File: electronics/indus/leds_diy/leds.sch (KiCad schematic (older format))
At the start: 21 parts, among them P1 LED+, P2 THERM, P3 LED-

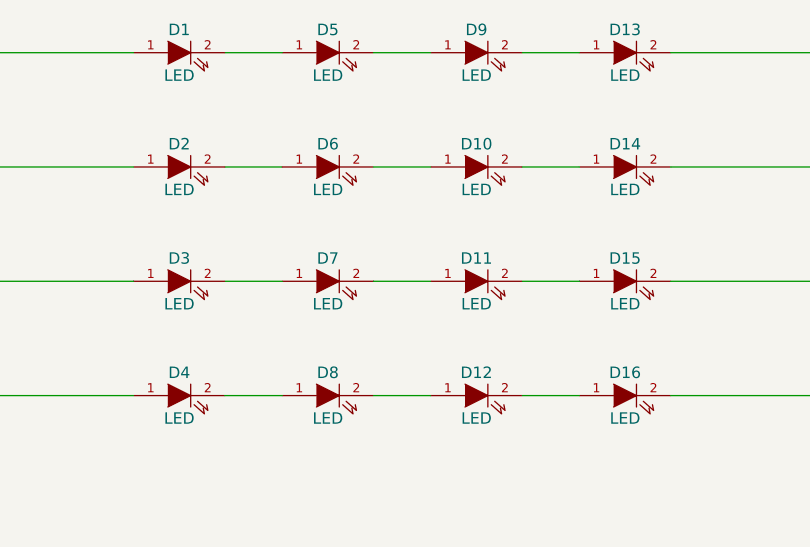
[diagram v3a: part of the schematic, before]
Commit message: led routing - one done
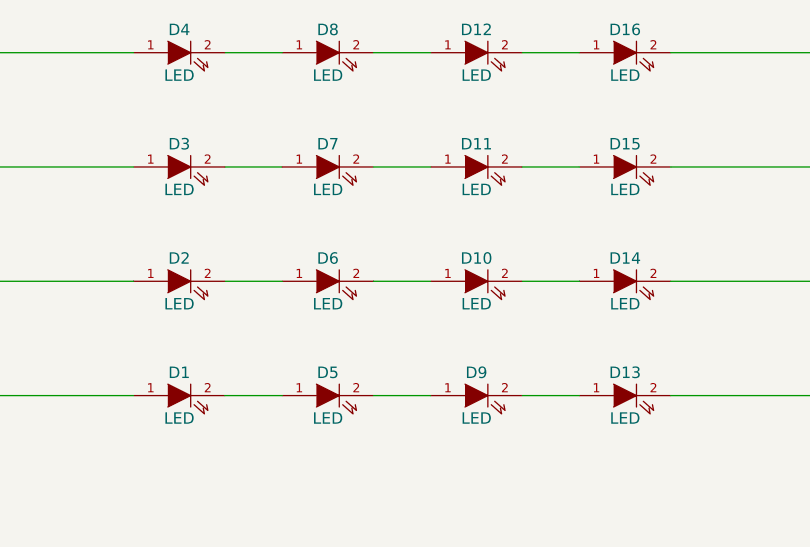
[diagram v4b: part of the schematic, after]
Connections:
- net at D1.1 (A): now also P1.1 (P1); no longer P1.4 (P4)
- net at D13.2 (K): now also P3.4 (P4); no longer P3.1 (P1)
- net at D2.1 (A): now also P1.2 (P2); no longer P1.3 (P3)
- net at D14.2 (K): now also P3.3 (P3); no longer P3.2 (P2)
- net at D3.1 (A): now also P1.3 (P3); no longer P1.2 (P2)
- net at D15.2 (K): now also P3.2 (P2); no longer P3.3 (P3)
- net at D4.1 (A): now also P1.4 (P4); no longer P1.1 (P1)
- net at D16.2 (K): now also P3.1 (P1); no longer P3.4 (P4)
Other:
- moved on the sheet: D1, D10, D11, D12, D13, D14, D15, D16, D2, D3, D4, D5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
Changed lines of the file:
@@
 L LED-RESCUE-leds D1
 U 1 1 56E1A1EF
+P 4750 3450
+F 0 "D1" H 4750 3550 50  0000 C CNN
+F 1 "LED" H 4750 3350 50  0000 C CNN
+F 2 "risebox:LUXEON-C" H 4750 3450 60  0001 C CNN
+F 3 "" H 4750 3450 60  0000 C CNN
+	1    4750 3450
+	1    0    0    -1
+$EndComp
+$Comp
+L LED-RESCUE-leds D5
+U 1 1 56E1A231
+P 5400 3450
+F 0 "D5" H 5400 3550 50  0000 C CNN
+F 1 "LED" H 5400 3350 50  0000 C CNN
+F 2 "risebox:LUXEON-C" H 5400 3450 60  0001 C CNN
+F 3 "" H 5400 3450 60  0000 C CNN
+	1    5400 3450
+	1    0    0    -1
+$EndComp
+$Comp
+L LED-RESCUE-leds D9
+U 1 1 56E1A294
+P 6050 3450
+F 0 "D9" H 6050 3550 50  0000 C CNN
+F 1 "LED" H 6050 3350 50  0000 C CNN
+F 2 "risebox:LUXEON-C" H 6050 3450 60  0001 C CNN
+F 3 "" H 6050 3450 60  0000 C CNN
+	1    6050 3450
+	1    0    0    -1
+$EndComp
+$Comp
+L LED-RESCUE-leds D13
+U 1 1 56E1A2C5
+P 6700 3450
+F 0 "D13" H 6700 3550 50  0000 C CNN
+F 1 "LED" H 6700 3350 50  0000 C CNN
+F 2 "risebox:LUXEON-C" H 6700 3450 60  0001 C CNN
+F 3 "" H 6700 3450 60  0000 C CNN
+	1    6700 3450
+	1    0    0    -1
+$EndComp
+$Comp
+L LED-RESCUE-leds D2
+U 1 1 56E1BEDB
+P 4750 2950
+F 0 "D2" H 4750 3050 50  0000 C CNN
+F 1 "LED" H 4750 2850 50  0000 C CNN
+F 2 "risebox:LUXEON-C" H 4750 2950 60  0001 C CNN
+F 3 "" H 4750 2950 60  0000 C CNN
+	1    4750 2950
+	1    0    0    -1
+$EndComp
+$Comp
+L LED-RESCUE-leds D6
+U 1 1 56E1BEE1
+P 5400 2950
+F 0 "D6" H 5400 3050 50  0000 C CNN
+F 1 "LED" H 5400 2850 50  0000 C CNN
+F 2 "risebox:LUXEON-C" H 5400 2950 60  0001 C CNN
+F 3 "" H 5400 2950 60  0000 C CNN
+	1    5400 2950
+	1    0    0    -1
+$EndComp
+$Comp
+L LED-RESCUE-leds D10
+U 1 1 56E1BEE7
+P 6050 2950
+F 0 "D10" H 6050 3050 50  0000 C CNN
+F 1 "LED" H 6050 2850 50  0000 C CNN
+F 2 "risebox:LUXEON-C" H 6050 2950 60  0001 C CNN
+F 3 "" H 6050 2950 60  0000 C CNN
+	1    6050 2950
+	1    0    0    -1
+$EndComp
+$Comp
+L LED-RESCUE-leds D14
+U 1 1 56E1BEED
+P 6700 2950
+F 0 "D14" H 6700 3050 50  0000 C CNN
+F 1 "LED" H 6700 2850 50  0000 C CNN
+F 2 "risebox:LUXEON-C" H 6700 2950 60  0001 C CNN
+F 3 "" H 6700 2950 60  0000 C CNN
+	1    6700 2950
+	1    0    0    -1
+$EndComp
+$Comp
+L LED-RESCUE-leds D3
+U 1 1 56E1C418
+P 4750 2450
+F 0 "D3" H 4750 2550 50  0000 C CNN
+F 1 "LED" H 4750 2350 50  0000 C CNN
+F 2 "risebox:LUXEON-C" H 4750 2450 60  0001 C CNN
+F 3 "" H 4750 2450 60  0000 C CNN
+	1    4750 2450
+	1    0    0    -1
+$EndComp
+$Comp
+L LED-RESCUE-leds D7
+U 1 1 56E1C41E
+P 5400 2450
+F 0 "D7" H 5400 2550 50  0000 C CNN
+F 1 "LED" H 5400 2350 50  0000 C CNN
+F 2 "risebox:LUXEON-C" H 5400 2450 60  0001 C CNN
+F 3 "" H 5400 2450 60  0000 C CNN
+	1    5400 2450
+	1    0    0    -1
+$EndComp
+$Comp
+L LED-RESCUE-leds D11
+U 1 1 56E1C424
+P 6050 2450
+F 0 "D11" H 6050 2550 50  0000 C CNN
+F 1 "LED" H 6050 2350 50  0000 C CNN
+F 2 "risebox:LUXEON-C" H 6050 2450 60  0001 C CNN
+F 3 "" H 6050 2450 60  0000 C CNN
+	1    6050 2450
+	1    0    0    -1
+$EndComp
+$Comp
+L LED-RESCUE-leds D15
+U 1 1 56E1C42A
+P 6700 2450
+F 0 "D15" H 6700 2550 50  0000 C CNN
+F 1 "LED" H 6700 2350 50  0000 C CNN
+F 2 "risebox:LUXEON-C" H 6700 2450 60  0001 C CNN
+F 3 "" H 6700 2450 60  0000 C CNN
+	1    6700 2450
+	1    0    0    -1
+$EndComp
+$Comp
+L LED-RESCUE-leds D4
+U 1 1 56E1C44F
 P 4750 1950
-F 0 "D1" H 4750 2050 50  0000 C CNN
+F 0 "D4" H 4750 2050 50  0000 C CNN
 F 1 "LED" H 4750 1850 50  0000 C CNN
 F 2 "risebox:LUXEON-C" H 4750 1950 60  0001 C CNN
@@
 $EndComp
 $Comp
-L LED-RESCUE-leds D5
-U 1 1 56E1A231
+L LED-RESCUE-leds D8
+U 1 1 56E1C455
 P 5400 1950
-F 0 "D5" H 5400 2050 50  0000 C CNN
+F 0 "D8" H 5400 2050 50  0000 C CNN
 F 1 "LED" H 5400 1850 50  0000 C CNN
 F 2 "risebox:LUXEON-C" H 5400 1950 60  0001 C CNN
@@
 $EndComp
 $Comp
-L LED-RESCUE-leds D9
-U 1 1 56E1A294
+L LED-RESCUE-leds D12
+U 1 1 56E1C45B
 P 6050 1950
-F 0 "D9" H 6050 2050 50  0000 C CNN
+F 0 "D12" H 6050 2050 50  0000 C CNN
 F 1 "LED" H 6050 1850 50  0000 C CNN
 F 2 "risebox:LUXEON-C" H 6050 1950 60  0001 C CNN
@@
 $EndComp
 $Comp
-L LED-RESCUE-leds D13
-U 1 1 56E1A2C5
+L LED-RESCUE-leds D16
+U 1 1 56E1C461
 P 6700 1950
-F 0 "D13" H 6700 2050 50  0000 C CNN
+F 0 "D16" H 6700 2050 50  0000 C CNN
 F 1 "LED" H 6700 1850 50  0000 C CNN
 F 2 "risebox:LUXEON-C" H 6700 1950 60  0001 C CNN
 F 3 "" H 6700 1950 60  0000 C CNN
 	1    6700 1950
-	1    0    0    -1
-$EndComp
-$Comp
-L LED-RESCUE-leds D2
-U 1 1 56E1BEDB
-P 4750 2450
-F 0 "D2" H 4750 2550 50  0000 C CNN
-F 1 "LED" H 4750 2350 50  0000 C CNN
-F 2 "risebox:LUXEON-C" H 4750 2450 60  0001 C CNN
-F 3 "" H 4750 2450 60  0000 C CNN
-	1    4750 2450
-	1    0    0    -1
-$EndComp
-$Comp
-L LED-RESCUE-leds D6
-U 1 1 56E1BEE1
-P 5400 2450
-F 0 "D6" H 5400 2550 50  0000 C CNN
-F 1 "LED" H 5400 2350 50  0000 C CNN
-F 2 "risebox:LUXEON-C" H 5400 2450 60  0001 C CNN
-F 3 "" H 5400 2450 60  0000 C CNN
-	1    5400 2450
-	1    0    0    -1
-$EndComp
-$Comp
-L LED-RESCUE-leds D10
-U 1 1 56E1BEE7
-P 6050 2450
-F 0 "D10" H 6050 2550 50  0000 C CNN
-F 1 "LED" H 6050 2350 50  0000 C CNN
-F 2 "risebox:LUXEON-C" H 6050 2450 60  0001 C CNN
-F 3 "" H 6050 2450 60  0000 C CNN
-	1    6050 2450
-	1    0    0    -1
-$EndComp
-$Comp
-L LED-RESCUE-leds D14
-U 1 1 56E1BEED
-P 6700 2450
-F 0 "D14" H 6700 2550 50  0000 C CNN
-F 1 "LED" H 6700 2350 50  0000 C CNN
-F 2 "risebox:LUXEON-C" H 6700 2450 60  0001 C CNN
-F 3 "" H 6700 2450 60  0000 C CNN
-	1    6700 2450
-	1    0    0    -1
-$EndComp
-$Comp
-L LED-RESCUE-leds D3
-U 1 1 56E1C418
-P 4750 2950
-F 0 "D3" H 4750 3050 50  0000 C CNN
-F 1 "LED" H 4750 2850 50  0000 C CNN
-F 2 "risebox:LUXEON-C" H 4750 2950 60  0001 C CNN
-F 3 "" H 4750 2950 60  0000 C CNN
-	1    4750 2950
-	1    0    0    -1
-$EndComp
-$Comp
-L LED-RESCUE-leds D7
-U 1 1 56E1C41E
-P 5400 2950
-F 0 "D7" H 5400 3050 50  0000 C CNN
-F 1 "LED" H 5400 2850 50  0000 C CNN
-F 2 "risebox:LUXEON-C" H 5400 2950 60  0001 C CNN
-F 3 "" H 5400 2950 60  0000 C CNN
-	1    5400 2950
-	1    0    0    -1
-$EndComp
-$Comp
-L LED-RESCUE-leds D11
-U 1 1 56E1C424
-P 6050 2950
-F 0 "D11" H 6050 3050 50  0000 C CNN
-F 1 "LED" H 6050 2850 50  0000 C CNN
-F 2 "risebox:LUXEON-C" H 6050 2950 60  0001 C CNN
-F 3 "" H 6050 2950 60  0000 C CNN
-	1    6050 2950
-	1    0    0    -1
-$EndComp
-$Comp
-L LED-RESCUE-leds D15
-U 1 1 56E1C42A
-P 6700 2950
-F 0 "D15" H 6700 3050 50  0000 C CNN
-F 1 "LED" H 6700 2850 50  0000 C CNN
-F 2 "risebox:LUXEON-C" H 6700 2950 60  0001 C CNN
-F 3 "" H 6700 2950 60  0000 C CNN
-	1    6700 2950
-	1    0    0    -1
-$EndComp
-$Comp
-L LED-RESCUE-leds D4
-U 1 1 56E1C44F
-P 4750 3450
-F 0 "D4" H 4750 3550 50  0000 C CNN
-F 1 "LED" H 4750 3350 50  0000 C CNN
-F 2 "risebox:LUXEON-C" H 4750 3450 60  0001 C CNN
-F 3 "" H 4750 3450 60  0000 C CNN
-	1    4750 3450
-	1    0    0    -1
-$EndComp
-$Comp
-L LED-RESCUE-leds D8
-U 1 1 56E1C455
-P 5400 3450
-F 0 "D8" H 5400 3550 50  0000 C CNN
-F 1 "LED" H 5400 3350 50  0000 C CNN
-F 2 "risebox:LUXEON-C" H 5400 3450 60  0001 C CNN
-F 3 "" H 5400 3450 60  0000 C CNN
-	1    5400 3450
-	1    0    0    -1
-$EndComp
-$Comp
-L LED-RESCUE-leds D12
-U 1 1 56E1C45B
-P 6050 3450
-F 0 "D12" H 6050 3550 50  0000 C CNN
-F 1 "LED" H 6050 3350 50  0000 C CNN
-F 2 "risebox:LUXEON-C" H 6050 3450 60  0001 C CNN
-F 3 "" H 6050 3450 60  0000 C CNN
-	1    6050 3450
-	1    0    0    -1
-$EndComp
-$Comp
-L LED-RESCUE-leds D16
-U 1 1 56E1C461
-P 6700 3450
-F 0 "D16" H 6700 3550 50  0000 C CNN
-F 1 "LED" H 6700 3350 50  0000 C CNN
-F 2 "risebox:LUXEON-C" H 6700 3450 60  0001 C CNN
-F 3 "" H 6700 3450 60  0000 C CNN
-	1    6700 3450
 	1    0    0    -1
 $EndComp
@@
 $EndComp
 Wire Wire Line
+	4950 3450 5200 3450
+Wire Wire Line
+	5600 3450 5850 3450
+Wire Wire Line
+	6250 3450 6500 3450
+Wire Wire Line
+	4950 2950 5200 2950
+Wire Wire Line
+	5600 2950 5850 2950
+Wire Wire Line
+	6250 2950 6500 2950
+Wire Wire Line
+	4950 2450 5200 2450
+Wire Wire Line
+	5600 2450 5850 2450
+Wire Wire Line
+	6250 2450 6500 2450
+Wire Wire Line
 	4950 1950 5200 1950
 Wire Wire Line
@@
 	6250 1950 6500 1950
 Wire Wire Line
-	4950 2450 5200 2450
-Wire Wire Line
-	5600 2450 5850 2450
-Wire Wire Line
-	6250 2450 6500 2450
-Wire Wire Line
-	4950 2950 5200 2950
-Wire Wire Line
-	5600 2950 5850 2950
-Wire Wire Line
-	6250 2950 6500 2950
-Wire Wire Line
-	4950 3450 5200 3450
-Wire Wire Line
-	5600 3450 5850 3450
-Wire Wire Line
-	6250 3450 6500 3450
-Wire Wire Line
 	2800 1950 4550 1950

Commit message: new connector footprint
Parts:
- P1, P3: footprint risebox:PINHEAD_LOCK_1-4 -> risebox:CONNECT_TE_3-647166-4
- P2: footprint risebox:PINHEAD_LOCK_1-3 -> risebox:CONNECT_TE_3-647166-3
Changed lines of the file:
@@
 F 0 "P1" H 1950 3000 50  0000 C CNN
 F 1 "LED+" V 2050 2750 50  0000 C CNN
-F 2 "risebox:PINHEAD_LOCK_1-4" H 1950 2750 60  0001 C CNN
+F 2 "risebox:CONNECT_TE_3-647166-4" H 1950 2750 60  0001 C CNN
 F 3 "" H 1950 2750 60  0000 C CNN
 	1    1950 2750
@@
 F 0 "P3" H 9200 2950 50  0000 C CNN
 F 1 "LED-" V 9300 2700 50  0000 C CNN
-F 2 "risebox:PINHEAD_LOCK_1-4" H 9200 2700 60  0001 C CNN
+F 2 "risebox:CONNECT_TE_3-647166-4" H 9200 2700 60  0001 C CNN
 F 3 "" H 9200 2700 60  0000 C CNN
 	1    9200 2700
@@
 F 0 "P2" H 5000 5200 50  0000 C CNN
 F 1 "THERM" V 5100 5000 50  0000 C CNN
-F 2 "risebox:PINHEAD_LOCK_1-3" H 5000 5000 60  0001 C CNN
+F 2 "risebox:CONNECT_TE_3-647166-3" H 5000 5000 60  0001 C CNN
 F 3 "" H 5000 5000 60  0000 C CNN
 	1    5000 5000
